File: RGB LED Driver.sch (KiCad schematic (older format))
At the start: 32 parts, among them J1 UART, J2 LED_STRIP_OUTPUT, J3 5V_POWER_INPUT, J4 PWR_BUTTON_TERMINAL, SW1 FLASH, SW2 MEM_RST, SW3 RESET, U1 ESP-12E, U2 AMS1117-3.3, U3 74LVC2G17

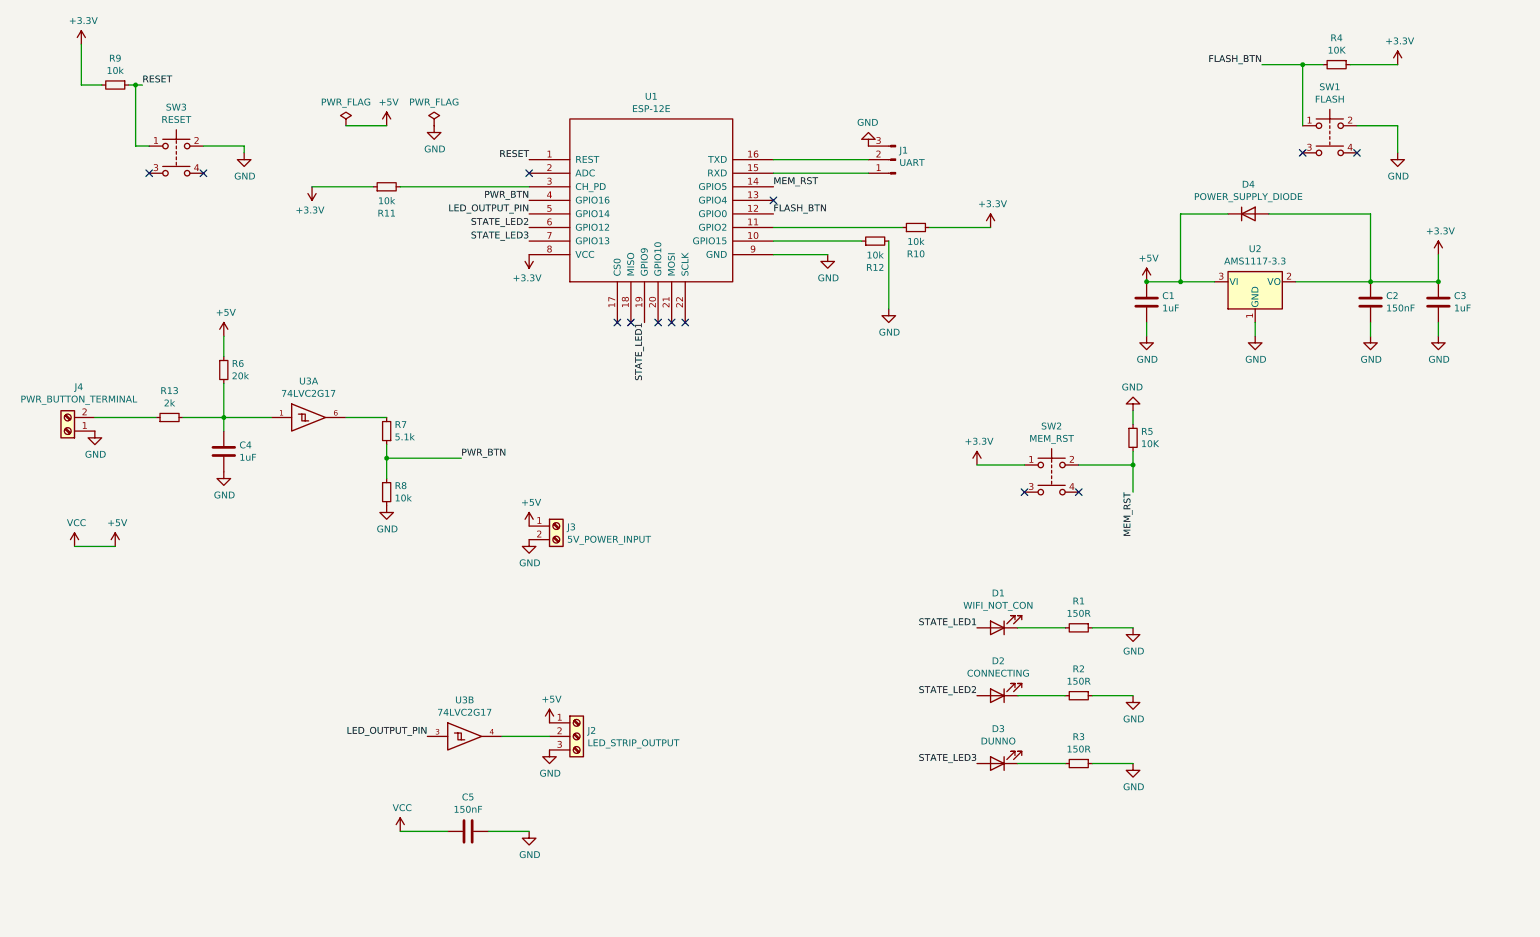
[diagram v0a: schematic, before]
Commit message: Working on PCB, bad footprint needs to be reworked
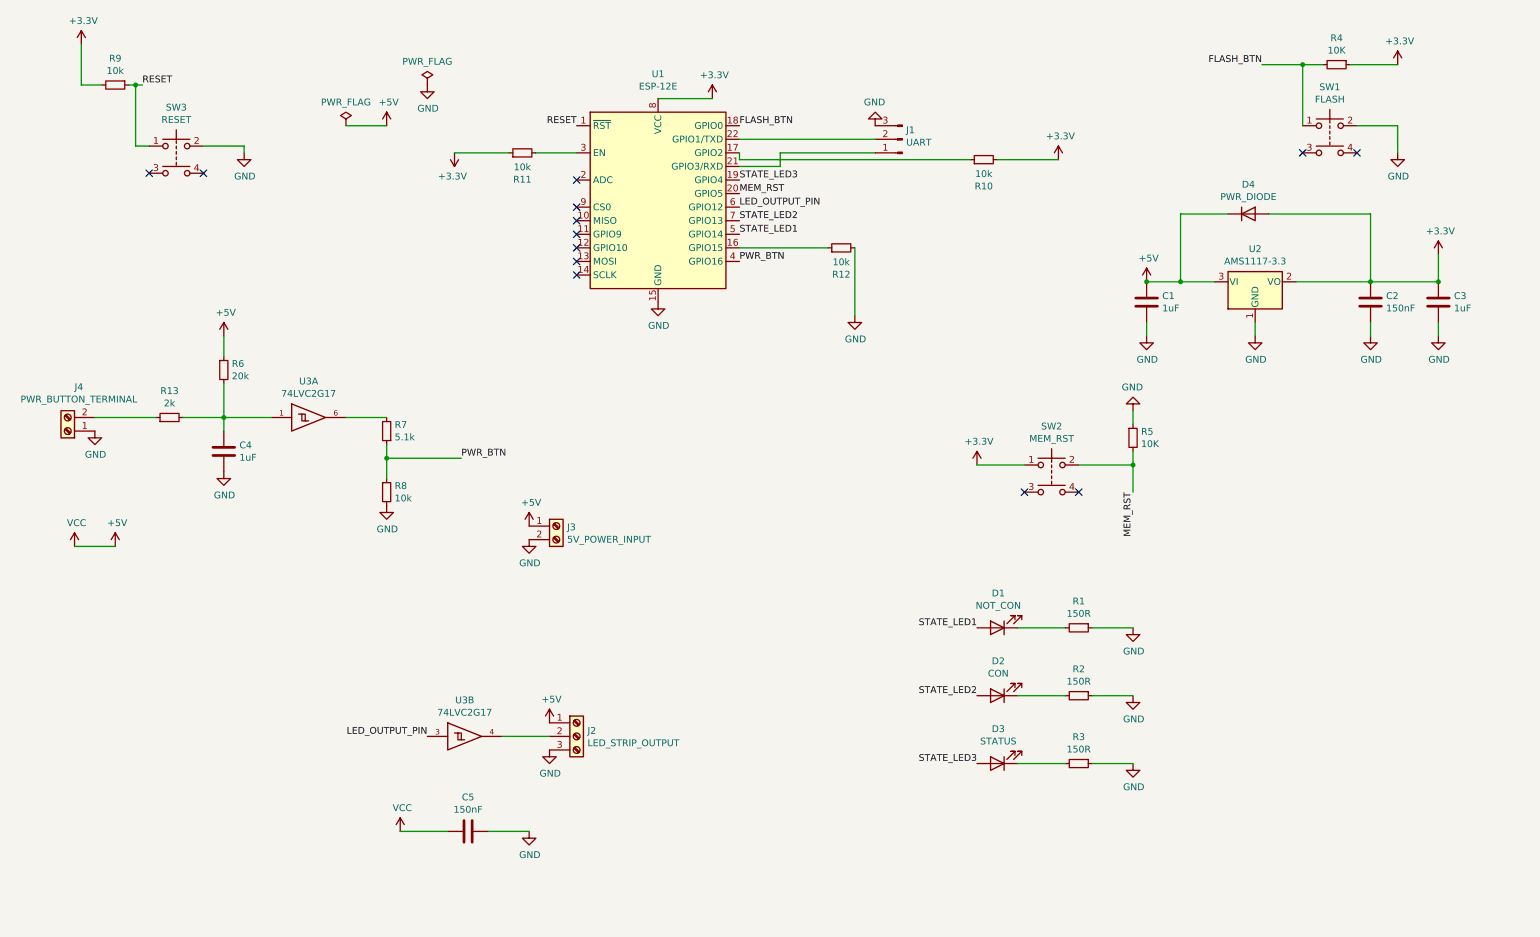
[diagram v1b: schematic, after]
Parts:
- removed U1: ESP-12E, RF_Module:ESP-12E, symbol ESP8266:ESP-12E
- added U1: ESP-12E, RF_Module:ESP-12E, symbol RF_Module:ESP-12E
- D1: value WIFI_NOT_CON -> NOT_CON
- D2: value CONNECTING -> CON
- D3: value DUNNO -> STATUS
- D4: value POWER_SUPPLY_DIODE -> PWR_DIODE
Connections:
- net +3V3: now also U1.8 (VCC)
- net FLASH_BTN: now also U1.18 (GPIO0)
- net GND: now also U1.15 (GND)
- net LED_OUTPUT_PIN: now also U1.6 (GPIO12)
- net MEM_RST: now also U1.20 (GPIO5)
- net PWR_BTN: now also U1.4 (GPIO16)
- net RESET: now also U1.1 (~RST)
- net STATE_LED1: now also U1.5 (GPIO14)
- net STATE_LED2: now also U1.7 (GPIO13)
- net STATE_LED3: now also U1.19 (GPIO4)
- net at R12.1: now also U1.16 (GPIO15)
- net at R10.1: now also U1.17 (GPIO2)
- net at J1.1 (Pin_1): now also U1.21 (GPIO3/RXD)
- net at J1.2 (Pin_2): now also U1.22 (GPIO1/TXD)
- net at R11.2: now also U1.3 (EN)
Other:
- moved on the sheet: J1, R10, R11, R12
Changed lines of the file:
@@
 Comment4 ""
 $EndDescr
-$Comp
-L ESP8266:ESP-12E U1
-U 1 1 6064BD32
-P 5150 1900
-F 0 "U1" H 5150 2665 50  0000 C CNN
-F 1 "ESP-12E" H 5150 2574 50  0000 C CNN
-F 2 "RF_Module:ESP-12E" H 5150 1900 50  0001 C CNN
-F 3 "http://l0l.org.uk/2014/12/esp8266-modules-hardware-guide-gotta-catch-em-all/" H 5150 1900 50  0001 C CNN
-	1    5150 1900
-	1    0    0    -1
-$EndComp
-NoConn ~ 5400 2800
-NoConn ~ 5300 2800
-NoConn ~ 5000 2800
-NoConn ~ 4900 2800
-$Comp
-L power:+3.3V #PWR0101
-U 1 1 6065D8F8
-P 4250 2300
-F 0 "#PWR0101" H 4250 2150 50  0001 C CNN
-F 1 "+3.3V" H 4265 2473 50  0000 C CNN
-F 2 "" H 4250 2300 50  0001 C CNN
-F 3 "" H 4250 2300 50  0001 C CNN
-	1    4250 2300
-	-1   0    0    1
-$EndComp
-NoConn ~ 4250 1700
+NoConn ~ 4600 2050
+NoConn ~ 4600 1950
+NoConn ~ 4600 1750
 $Comp
 L Device:R_Small R9
@@
 L power:+3.3V #PWR0105
 U 1 1 6068A443
-P 7650 2100
-F 0 "#PWR0105" H 7650 1950 50  0001 C CNN
-F 1 "+3.3V" H 7665 2273 50  0000 C CNN
-F 2 "" H 7650 2100 50  0001 C CNN
-F 3 "" H 7650 2100 50  0001 C CNN
-	1    7650 2100
+P 8150 1600
+F 0 "#PWR0105" H 8150 1450 50  0001 C CNN
+F 1 "+3.3V" H 8165 1773 50  0000 C CNN
+F 2 "" H 8150 1600 50  0001 C CNN
+F 3 "" H 8150 1600 50  0001 C CNN
+	1    8150 1600
 	1    0    0    -1
 $EndComp
@@
 L Device:R_Small R10
 U 1 1 6069493B
-P 7100 2100
-F 0 "R10" V 6904 2100 50  0000 C CNN
-F 1 "10k" V 6995 2100 50  0000 C CNN
-F 2 "Resistor_SMD:R_0805_2012Metric_Pad1.20x1.40mm_HandSolder" H 7100 2100 50  0001 C CNN
-F 3 "~" H 7100 2100 50  0001 C CNN
-	1    7100 2100
+P 7600 1600
+F 0 "R10" V 7404 1600 50  0000 C CNN
+F 1 "10k" V 7495 1600 50  0000 C CNN
+F 2 "Resistor_SMD:R_0805_2012Metric_Pad1.20x1.40mm_HandSolder" H 7600 1600 50  0001 C CNN
+F 3 "~" H 7600 1600 50  0001 C CNN
+	1    7600 1600
 	0    -1   -1   0
 $EndComp
 Wire Wire Line
-	7200 2100 7650 2100
+	7700 1600 8150 1600
 $Comp
 L Device:R_Small R11
 U 1 1 60696851
-P 3200 1800
-F 0 "R11" V 3004 1800 50  0000 C CNN
-F 1 "10k" V 3095 1800 50  0000 C CNN
-F 2 "Resistor_SMD:R_0805_2012Metric_Pad1.20x1.40mm_HandSolder" H 3200 1800 50  0001 C CNN
-F 3 "~" H 3200 1800 50  0001 C CNN
-	1    3200 1800
+P 4200 1550
+F 0 "R11" V 4004 1550 50  0000 C CNN
+F 1 "10k" V 4095 1550 50  0000 C CNN
+F 2 "Resistor_SMD:R_0805_2012Metric_Pad1.20x1.40mm_HandSolder" H 4200 1550 50  0001 C CNN
+F 3 "~" H 4200 1550 50  0001 C CNN
+	1    4200 1550
 	0    -1   -1   0
 $EndComp
@@
 L power:+3.3V #PWR0106
 U 1 1 606970BA
-P 2650 1800
-F 0 "#PWR0106" H 2650 1650 50  0001 C CNN
-F 1 "+3.3V" H 2665 1973 50  0000 C CNN
-F 2 "" H 2650 1800 50  0001 C CNN
-F 3 "" H 2650 1800 50  0001 C CNN
-	1    2650 1800
+P 3700 1550
+F 0 "#PWR0106" H 3700 1400 50  0001 C CNN
+F 1 "+3.3V" H 3715 1723 50  0000 C CNN
+F 2 "" H 3700 1550 50  0001 C CNN
+F 3 "" H 3700 1550 50  0001 C CNN
+	1    3700 1550
 	-1   0    0    1
 $EndComp
 Wire Wire Line
-	2650 1800 3100 1800
+	3700 1550 4100 1550
 $Comp
 L Device:R_Small R12
 U 1 1 6069A2FC
-P 6800 2200
-F 0 "R12" V 6604 2200 50  0000 C CNN
-F 1 "10k" V 6695 2200 50  0000 C CNN
-F 2 "Resistor_SMD:R_0805_2012Metric_Pad1.20x1.40mm_HandSolder" H 6800 2200 50  0001 C CNN
-F 3 "~" H 6800 2200 50  0001 C CNN
-	1    6800 2200
+P 6550 2250
+F 0 "R12" V 6354 2250 50  0000 C CNN
+F 1 "10k" V 6445 2250 50  0000 C CNN
+F 2 "Resistor_SMD:R_0805_2012Metric_Pad1.20x1.40mm_HandSolder" H 6550 2250 50  0001 C CNN
+F 3 "~" H 6550 2250 50  0001 C CNN
+	1    6550 2250
 	0    -1   -1   0
 $EndComp
@@
 L power:GND #PWR0107
 U 1 1 6069A849
-P 6900 2700
-F 0 "#PWR0107" H 6900 2450 50  0001 C CNN
-F 1 "GND" H 6905 2527 50  0000 C CNN
-F 2 "" H 6900 2700 50  0001 C CNN
-F 3 "" H 6900 2700 50  0001 C CNN
-	1    6900 2700
+P 6650 2750
+F 0 "#PWR0107" H 6650 2500 50  0001 C CNN
+F 1 "GND" H 6655 2577 50  0000 C CNN
+F 2 "" H 6650 2750 50  0001 C CNN
+F 3 "" H 6650 2750 50  0001 C CNN
+	1    6650 2750
 	1    0    0    -1
 $EndComp
@@
 P 7700 5050
 F 0 "D1" H 7693 4795 50  0000 C CNN
-F 1 "WIFI_NOT_CON" H 7693 4886 50  0000 C CNN
+F 1 "NOT_CON" H 7693 4886 50  0000 C CNN
 F 2 "LED_SMD:LED_0805_2012Metric_Pad1.15x1.40mm_HandSolder" H 7700 5050 50  0001 C CNN
 F 3 "~" H 7700 5050 50  0001 C CNN
@@
 P 7700 5550
 F 0 "D2" H 7693 5295 50  0000 C CNN
-F 1 "CONNECTING" H 7693 5386 50  0000 C CNN
+F 1 "CON" H 7693 5386 50  0000 C CNN
 F 2 "LED_SMD:LED_0805_2012Metric_Pad1.15x1.40mm_HandSolder" H 7700 5550 50  0001 C CNN
 F 3 "~" H 7700 5550 50  0001 C CNN
@@
 P 7700 6050
 F 0 "D3" H 7693 5795 50  0000 C CNN
-F 1 "DUNNO" H 7693 5886 50  0000 C CNN
+F 1 "STATUS" H 7693 5886 50  0000 C CNN
 F 2 "LED_SMD:LED_0805_2012Metric_Pad1.15x1.40mm_HandSolder" H 7700 6050 50  0001 C CNN
 F 3 "~" H 7700 6050 50  0001 C CNN
@@
 Wire Wire Line
 	8400 5050 8700 5050
-NoConn ~ 5200 2800
-NoConn ~ 6050 1900
 Wire Wire Line
 	8700 3550 8700 3450
@@
 Wire Wire Line
 	2000 2900 2000 3050
-$Comp
-L power:GND #PWR0104
-U 1 1 60A1ED7A
-P 6450 2300
-F 0 "#PWR0104" H 6450 2050 50  0001 C CNN
-F 1 "GND" H 6455 2127 50  0000 C CNN
-F 2 "" H 6450 2300 50  0001 C CNN
-F 3 "" H 6450 2300 50  0001 C CNN
-	1    6450 2300
-	1    0    0    -1
-$EndComp
-Wire Wire Line
-	6450 2300 6050 2300
 Wire Wire Line
 	8700 6050 8400 6050
@@
 L power:GND #PWR0131
 U 1 1 60A71088
-P 3550 1350
-F 0 "#PWR0131" H 3550 1100 50  0001 C CNN
-F 1 "GND" H 3555 1177 50  0000 C CNN
-F 2 "" H 3550 1350 50  0001 C CNN
-F 3 "" H 3550 1350 50  0001 C CNN
-	1    3550 1350
+P 3500 1050
+F 0 "#PWR0131" H 3500 800 50  0001 C CNN
+F 1 "GND" H 3505 877 50  0000 C CNN
+F 2 "" H 3500 1050 50  0001 C CNN
+F 3 "" H 3500 1050 50  0001 C CNN
+	1    3500 1050
 	1    0    0    -1
 $EndComp
@@
 L power:PWR_FLAG #FLG0102
 U 1 1 60A715F9
-P 3550 1350
-F 0 "#FLG0102" H 3550 1425 50  0001 C CNN
-F 1 "PWR_FLAG" H 3550 1523 50  0000 C CNN
-F 2 "" H 3550 1350 50  0001 C CNN
-F 3 "~" H 3550 1350 50  0001 C CNN
-	1    3550 1350
+P 3500 1050
+F 0 "#FLG0102" H 3500 1125 50  0001 C CNN
+F 1 "PWR_FLAG" H 3500 1223 50  0000 C CNN
+F 2 "" H 3500 1050 50  0001 C CNN
+F 3 "~" H 3500 1050 50  0001 C CNN
+	1    3500 1050
 	1    0    0    -1
 $EndComp
@@
 L Connector:Conn_01x03_Male J1
 U 1 1 60B57316
-P 6950 1600
-F 0 "J1" H 6922 1532 50  0000 R CNN
-F 1 "UART" H 6922 1623 50  0000 R CNN
-F 2 "Connector_PinSocket_2.54mm:PinSocket_1x03_P2.54mm_Vertical" H 6950 1600 50  0001 C CNN
-F 3 "~" H 6950 1600 50  0001 C CNN
-	1    6950 1600
+P 7000 1450
+F 0 "J1" H 6972 1382 50  0000 R CNN
+F 1 "UART" H 6972 1473 50  0000 R CNN
+F 2 "Connector_PinSocket_2.54mm:PinSocket_1x03_P2.54mm_Vertical" H 7000 1450 50  0001 C CNN
+F 3 "~" H 7000 1450 50  0001 C CNN
+	1    7000 1450
 	-1   0    0    1
 $EndComp
@@
 L power:GND #PWR0132
 U 1 1 60B5814E
-P 6750 1500
-F 0 "#PWR0132" H 6750 1250 50  0001 C CNN
-F 1 "GND" H 6755 1327 50  0000 C CNN
-F 2 "" H 6750 1500 50  0001 C CNN
-F 3 "" H 6750 1500 50  0001 C CNN
-	1    6750 1500
+P 6800 1350
+F 0 "#PWR0132" H 6800 1100 50  0001 C CNN
+F 1 "GND" H 6805 1177 50  0000 C CNN
+F 2 "" H 6800 1350 50  0001 C CNN
+F 3 "" H 6800 1350 50  0001 C CNN
+	1    6800 1350
 	-1   0    0    1
 $EndComp
@@
 Wire Wire Line
 	1700 3500 2000 3500
-Wire Wire Line
-	6050 1700 6750 1700
-Wire Wire Line
-	6750 1600 6050 1600
 Text Label 7550 5050 2    50   ~ 0
 STATE_LED1
@@
 Text Label 7550 6050 2    50   ~ 0
 STATE_LED3
-Text Label 5100 2800 3    50   ~ 0
+Text Label 5800 2150 0    50   ~ 0
 STATE_LED1
-Text Label 4250 2100 2    50   ~ 0
+Text Label 5800 2050 0    50   ~ 0
 STATE_LED2
-Text Label 4250 2200 2    50   ~ 0
+Text Label 5800 1750 0    50   ~ 0
 STATE_LED3
-Text Label 4250 1600 2    50   ~ 0
+Text Label 4600 1350 2    50   ~ 0
 RESET
-Text Label 4250 1900 2    50   ~ 0
+Text Label 5800 2350 0    50   ~ 0
 PWR_BTN
-Text Label 4250 2000 2    50   ~ 0
+Text Label 5800 1950 0    50   ~ 0
 LED_OUTPUT_PIN
 Text Label 1400 1050 0    50   ~ 0
@@
 Text Label 3750 3800 0    50   ~ 0
 PWR_BTN
-Text Label 6050 1800 0    50   ~ 0
+Text Label 5800 1850 0    50   ~ 0
 MEM_RST
 Text Label 8700 4050 3    50   ~ 0
@@
 P 9550 2000
 F 0 "D4" H 9550 2217 50  0000 C CNN
-F 1 "POWER_SUPPLY_DIODE" H 9550 2126 50  0000 C CNN
+F 1 "PWR_DIODE" H 9550 2126 50  0000 C CNN
 F 2 "Diode_SMD:D_MiniMELF_Handsoldering" H 9550 2000 50  0001 C CNN
 F 3 "~" H 9550 2000 50  0001 C CNN
@@
 	4050 5850 4400 5850
 Wire Wire Line
-	6050 2200 6700 2200
-Wire Wire Line
-	6900 2200 6900 2700
-Wire Wire Line
-	6050 2100 7000 2100
-Wire Wire Line
-	3300 1800 4250 1800
-Text Label 6050 2000 0    50   ~ 0
+	5800 2250 6450 2250
+Wire Wire Line
+	6650 2250 6650 2750
+Text Label 5800 1350 0    50   ~ 0
 FLASH_BTN
 Text Label 9650 900  2    50   ~ 0
@@
 $EndComp
 Connection ~ 10950 2500
+Wire Wire Line
+	6800 1550 6100 1550
+Wire Wire Line
+	4300 1550 4600 1550
+$Comp
+L RF_Module:ESP-12E U1
+U 1 1 606E886D
+P 5200 1950
+F 0 "U1" H 5200 2931 50  0000 C CNN
+F 1 "ESP-12E" H 5200 2840 50  0000 C CNN
+F 2 "RF_Module:ESP-12E" H 5200 1950 50  0001 C CNN
+F 3 "http://wiki.ai-thinker.com/_media/esp8266/esp8266_series_modules_user_manual_v1.1.pdf" H 4850 2050 50  0001 C CNN
+	1    5200 1950
+	1    0    0    -1
+$EndComp
+NoConn ~ 4600 2250
+NoConn ~ 4600 2350
+NoConn ~ 4600 2450
+$Comp
+L power:GND #PWR0101
+U 1 1 6075B377
+P 5200 2650
+F 0 "#PWR0101" H 5200 2400 50  0001 C CNN
+F 1 "GND" H 5205 2477 50  0000 C CNN
+F 2 "" H 5200 2650 50  0001 C CNN
+F 3 "" H 5200 2650 50  0001 C CNN
+	1    5200 2650
+	1    0    0    -1
+$EndComp
+Wire Wire Line
+	5800 1450 6800 1450
+Wire Wire Line
+	6100 1550 6100 1650
+Wire Wire Line
+	6100 1650 5800 1650
+Wire Wire Line
+	5800 1600 5800 1550
+Wire Wire Line
+	5800 1600 7500 1600
+$Comp
+L power:+3.3V #PWR0104
+U 1 1 60714123
+P 5600 1150
+F 0 "#PWR0104" H 5600 1000 50  0001 C CNN
+F 1 "+3.3V" H 5615 1323 50  0000 C CNN
+F 2 "" H 5600 1150 50  0001 C CNN
+F 3 "" H 5600 1150 50  0001 C CNN
+	1    5600 1150
+	1    0    0    -1
+$EndComp
+Wire Wire Line
+	5200 1150 5600 1150
+NoConn ~ 4600 2150
 $EndSCHEMATC

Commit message: Done 1st version of PCB
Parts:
- removed SW1: FLASH, Button_Switch_SMD:SW_Push_1P1T_NO_6x6mm_H9.5mm, symbol Switch:SW_Push_Dual
- removed SW2: MEM_RST, Button_Switch_SMD:SW_Push_1P1T_NO_6x6mm_H9.5mm, symbol Switch:SW_Push_Dual
- removed SW3: RESET, Button_Switch_SMD:SW_Push_1P1T_NO_6x6mm_H9.5mm, symbol Switch:SW_Push_Dual
- added SW1, SW2, SW3: SW_Push, Button_Switch_SMD:SW_Push_1P1T_NO_6x6mm_H9.5mm, symbol Switch:SW_Push
- J4: value PWR_BUTTON_TERMINAL -> PWR_BTN
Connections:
- net +3V3: now also SW2.1
- net FLASH_BTN: now also SW1.1
- net GND: now also SW1.2, SW3.2
- net MEM_RST: now also SW2.2
- net RESET: now also SW3.1
- no-connect marks 13 -> 7
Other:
- moved on the sheet: C1, C2, C3, C4, C5, D1, D2, D3, D4, J1, J2, J3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
